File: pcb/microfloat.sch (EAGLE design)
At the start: 130 parts, among them J1 503182-1852, J11 JTAG-MINI, J2 USB4105_REVA, J3 1054291110, J4 1054291110, J5 1054291116, J9 1909763-1, T1 MMBT3906, U1 BME280, U12 TPS54308DDCT, U13 TPS54308DDCT, U2 ICM-42688-P, U3 MAX13237EETE, U4 NEO-M8N-0, U5 TXB0104PWR, U6 LTC4419CMSEPBF, U7 TPS54308DDCT, U8 TPS54308DDCT, U9 ATSAMD51N20A-AUT, Y1 32.768kHz

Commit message: part of component placement done
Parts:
- added C41: 10uF, rcl:CPOL-USE2.5-5
- added C42: 100uF, rcl:CPOL-USE3.5-8
- added C43, C44: 0.1uF, rcl:C-USC0603
- added F6: 0.6A, microfloat:SMD_FUSE1206
- renumbered J11 to J6
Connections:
- removed net GND1: C11.2, C12.2, C29.2, C30.2, C8.2
- new net N$27: C41.+, C42.+, F6.1
- new net N$29: J6.GND@1
- net +3V3: now also C43.1, C44.1
- net GND: now also C11.2, C12.2, C29.2, C30.2, C41.-, C42.-, C43.2, C44.2, C8.2; no longer J6.GND@1
- net VBATT: now also F6.2
- net XIN32: now also U9.PA00
- net XOUT32: now also U9.PA01
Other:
- moved on the sheet: C26, C33, C34, C35, C36, C37, C38, C39, L1

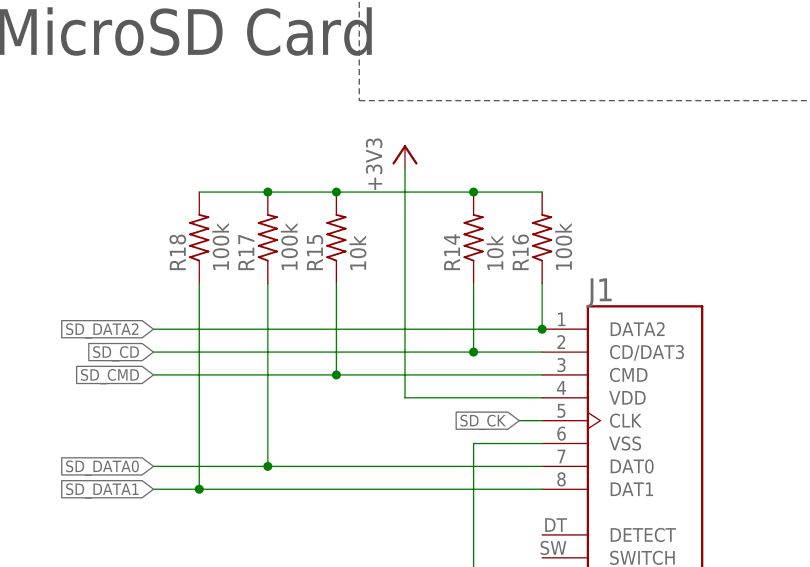
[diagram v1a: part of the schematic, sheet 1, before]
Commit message: component placement near complete, need to fix connector, place test points
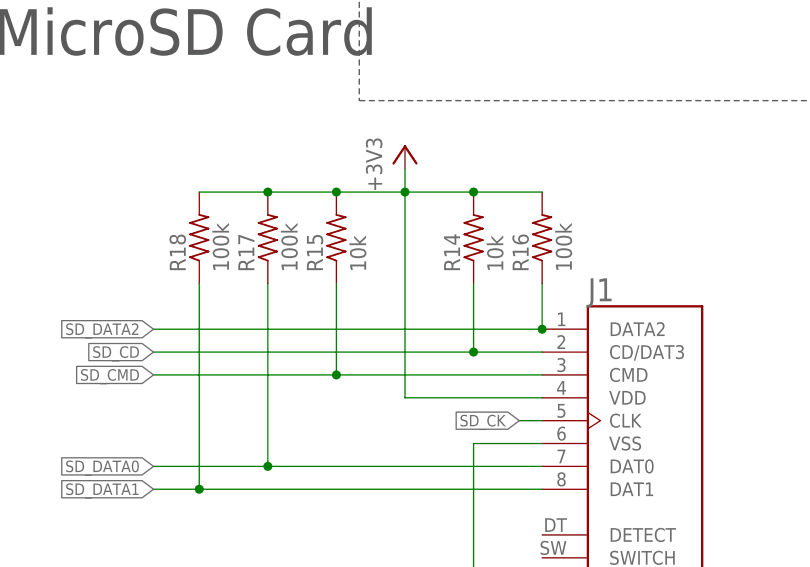
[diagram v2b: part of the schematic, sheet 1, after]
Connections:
- removed net N$25: R14.2, R15.2, R16.2, R17.2, R18.2
- net +3V3: now also R14.2, R15.2, R16.2, R17.2, R18.2
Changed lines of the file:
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@@
 <part name="F5" library="microfloat" deviceset="SMD_FUSE" device="1206" value="0.5A"/>
 <part name="U$29" library="microfloat" deviceset="TEST_POINT" device=""/>
-<part name="U$30" library="microfloat" deviceset="VBATT_5V" device=""/>
 <part name="U$31" library="microfloat" deviceset="TEST_POINT" device=""/>
 <part name="U$32" library="microfloat" deviceset="TEST_POINT" device=""/>
@@
 <part name="J6" library="microfloat" deviceset="JTAG-MINI" device=""/>
 <part name="GND18" library="supply1" library_urn="urn:adsk.eagle:library:371" deviceset="GND" device=""/>
+<part name="U$16" library="microfloat" deviceset="VBATT_5V" device=""/>
 </parts>
 <sheets>
@@
 <pinref part="J1" gate="G$1" pin="VDD"/>
 <wire x1="233.68" y1="187.96" x2="218.44" y2="187.96" width="0.1524" layer="91"/>
-<wire x1="218.44" y1="187.96" x2="218.44" y2="213.36" width="0.1524" layer="91"/>
+<wire x1="218.44" y1="187.96" x2="218.44" y2="210.82" width="0.1524" layer="91"/>
 <pinref part="+3V15" gate="G$1" pin="+3V3"/>
+<pinref part="R16" gate="G$1" pin="2"/>
+<pinref part="R18" gate="G$1" pin="2"/>
+<wire x1="218.44" y1="210.82" x2="218.44" y2="213.36" width="0.1524" layer="91"/>
+<wire x1="233.68" y1="210.82" x2="226.06" y2="210.82" width="0.1524" layer="91"/>
+<pinref part="R14" gate="G$1" pin="2"/>
+<wire x1="226.06" y1="210.82" x2="218.44" y2="210.82" width="0.1524" layer="91"/>
+<junction x="226.06" y="210.82"/>
+<pinref part="R15" gate="G$1" pin="2"/>
+<wire x1="218.44" y1="210.82" x2="210.82" y2="210.82" width="0.1524" layer="91"/>
+<wire x1="210.82" y1="210.82" x2="203.2" y2="210.82" width="0.1524" layer="91"/>
+<junction x="210.82" y="210.82"/>
+<pinref part="R17" gate="G$1" pin="2"/>
+<wire x1="203.2" y1="210.82" x2="195.58" y2="210.82" width="0.1524" layer="91"/>
+<junction x="203.2" y="210.82"/>
+<junction x="218.44" y="210.82"/>
 </segment>
 <segment>
@@
 </segment>
 </net>
-<net name="N$25" class="0">
-<segment>
-<pinref part="R16" gate="G$1" pin="2"/>
-<pinref part="R18" gate="G$1" pin="2"/>
-<wire x1="233.68" y1="210.82" x2="226.06" y2="210.82" width="0.1524" layer="91"/>
-<pinref part="R14" gate="G$1" pin="2"/>
-<wire x1="226.06" y1="210.82" x2="210.82" y2="210.82" width="0.1524" layer="91"/>
-<junction x="226.06" y="210.82"/>
-<pinref part="R15" gate="G$1" pin="2"/>
-<wire x1="210.82" y1="210.82" x2="203.2" y2="210.82" width="0.1524" layer="91"/>
-<junction x="210.82" y="210.82"/>
-<pinref part="R17" gate="G$1" pin="2"/>
-<wire x1="203.2" y1="210.82" x2="195.58" y2="210.82" width="0.1524" layer="91"/>
-<junction x="203.2" y="210.82"/>
-</segment>
-</net>
 <net name="MOSI_1" class="0">
 <segment>
@@
 </instance>
 <instance part="U$29" gate="G$1" x="157.48" y="180.34" smashed="yes"/>
-<instance part="U$30" gate="G$1" x="381" y="264.16" smashed="yes">
-<attribute name="VALUE" x="378.46" y="261.62" size="1.778" layer="96" rot="R90"/>
-</instance>
 <instance part="U$31" gate="G$1" x="241.3" y="149.86" smashed="yes"/>
 <instance part="U$32" gate="G$1" x="284.48" y="157.48" smashed="yes"/>
@@
 <attribute name="VALUE" x="340.36" y="180.34" size="1.778" layer="96" rot="R90"/>
 </instance>
+<instance part="U$16" gate="G$1" x="381" y="264.16" smashed="yes">
+<attribute name="VALUE" x="378.46" y="261.62" size="1.778" layer="96" rot="R90"/>
+</instance>
 </instances>
 <busses>
@@
 </segment>
 </net>
-<net name="N$19" class="0">
-<segment>
-<pinref part="R10" gate="G$1" pin="2"/>
-<wire x1="370.84" y1="238.76" x2="370.84" y2="236.22" width="0.1524" layer="91"/>
-<wire x1="370.84" y1="238.76" x2="381" y2="238.76" width="0.1524" layer="91"/>
-<junction x="370.84" y="238.76"/>
-<pinref part="L2" gate="A" pin="2"/>
-<wire x1="363.22" y1="238.76" x2="370.84" y2="238.76" width="0.1524" layer="91"/>
-<wire x1="381" y1="238.76" x2="381" y2="228.6" width="0.1524" layer="91"/>
-<pinref part="C19" gate="G$1" pin="1"/>
-<wire x1="381" y1="238.76" x2="391.16" y2="238.76" width="0.1524" layer="91"/>
-<wire x1="391.16" y1="238.76" x2="391.16" y2="228.6" width="0.1524" layer="91"/>
-<pinref part="C20" gate="G$1" pin="1"/>
-<junction x="381" y="238.76"/>
-<pinref part="F4" gate="G$1" pin="1"/>
-</segment>
-</net>
 <net name="N$20" class="0">
 <segment>
@@
 </segment>
 <segment>
-<pinref part="F4" gate="G$1" pin="2"/>
-<wire x1="381" y1="261.62" x2="381" y2="259.08" width="0.1524" layer="91"/>
 <pinref part="U$9" gate="G$1" pin="P$1"/>
+<pinref part="F4" gate="G$1" pin="2"/>
+<pinref part="U$16" gate="G$1" pin="VBATT_5V"/>
+<wire x1="381" y1="259.08" x2="381" y2="261.62" width="0.1524" layer="91"/>
 <junction x="381" y="259.08"/>
-<pinref part="U$30" gate="G$1" pin="VBATT_5V"/>
 </segment>
 </net>
@@
 </segment>
 </net>
+<net name="N$19" class="0">
+<segment>
+<wire x1="391.16" y1="238.76" x2="391.16" y2="228.6" width="0.1524" layer="91"/>
+<pinref part="C20" gate="G$1" pin="1"/>
+<pinref part="R10" gate="G$1" pin="2"/>
+<wire x1="370.84" y1="238.76" x2="370.84" y2="236.22" width="0.1524" layer="91"/>
+<pinref part="L2" gate="A" pin="2"/>
+<wire x1="363.22" y1="238.76" x2="370.84" y2="238.76" width="0.1524" layer="91"/>
+<pinref part="C19" gate="G$1" pin="1"/>
+<pinref part="F4" gate="G$1" pin="1"/>
+<wire x1="381" y1="228.6" x2="381" y2="238.76" width="0.1524" layer="91"/>
+<wire x1="370.84" y1="238.76" x2="381" y2="238.76" width="0.1524" layer="91"/>
+<junction x="370.84" y="238.76"/>
+<junction x="381" y="238.76"/>
+<wire x1="391.16" y1="238.76" x2="381" y2="238.76" width="0.1524" layer="91"/>
+</segment>
+</net>

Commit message: Work in progress
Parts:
- removed L1: 380hm, RoboJackets-Inductors:INDUCTOR_0805
- added C45, C46: 0.1uF, rcl:C-USC0603
- C15, C16: value 15 pF -> 8.2 pF
- C41, C42: TOLERANCE (none) -> 20%; VOLTAGE (none) -> 35V
- F6: value 0.6A -> 3A
- R1: TOLERANCE (none) -> 1%
- R8, R9: TOLERANCE 1% -> 0.1%
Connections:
- removed net N$29: J6.GND@1
- removed net N$30: J4.11
- net +3V3: now also C36.1, C37.1, C45.1, C46.1; no longer L1.1
- net GND: now also C45.2, C46.2, J4.11, J6.GND@1
- net VCCA: no longer C36.1, C37.1, L1.2

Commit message: Put final crystal part
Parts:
- added C47: 10uF, rcl:C-USC0603
- added C48: 0.1uF, rcl:C-USC0603
- added L1: FB-30Ohm, RoboJackets-Inductors:INDUCTOR_0805
- added L4: 10uH, RoboJackets-Inductors:INDUCTOR_0805
- C15, C16: TOLERANCE (none) -> 0.5%; VOLTAGE (none) -> 10V
- C32, C33, C34, C43, C44: TOLERANCE (none) -> 5%; VOLTAGE (none) -> 10V
- C36: value 0.1uF -> 10uF
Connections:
- new net GND1: C47.2
- new net GND2: C48.2
- new net N$25: L4.1, U9.VSW
- net +3V3: now also L1.1
- net VCCA: now also C47.1, C48.1, L1.2
- net VCC_CORE: now also L4.2
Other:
- moved on the sheet: C38, C39

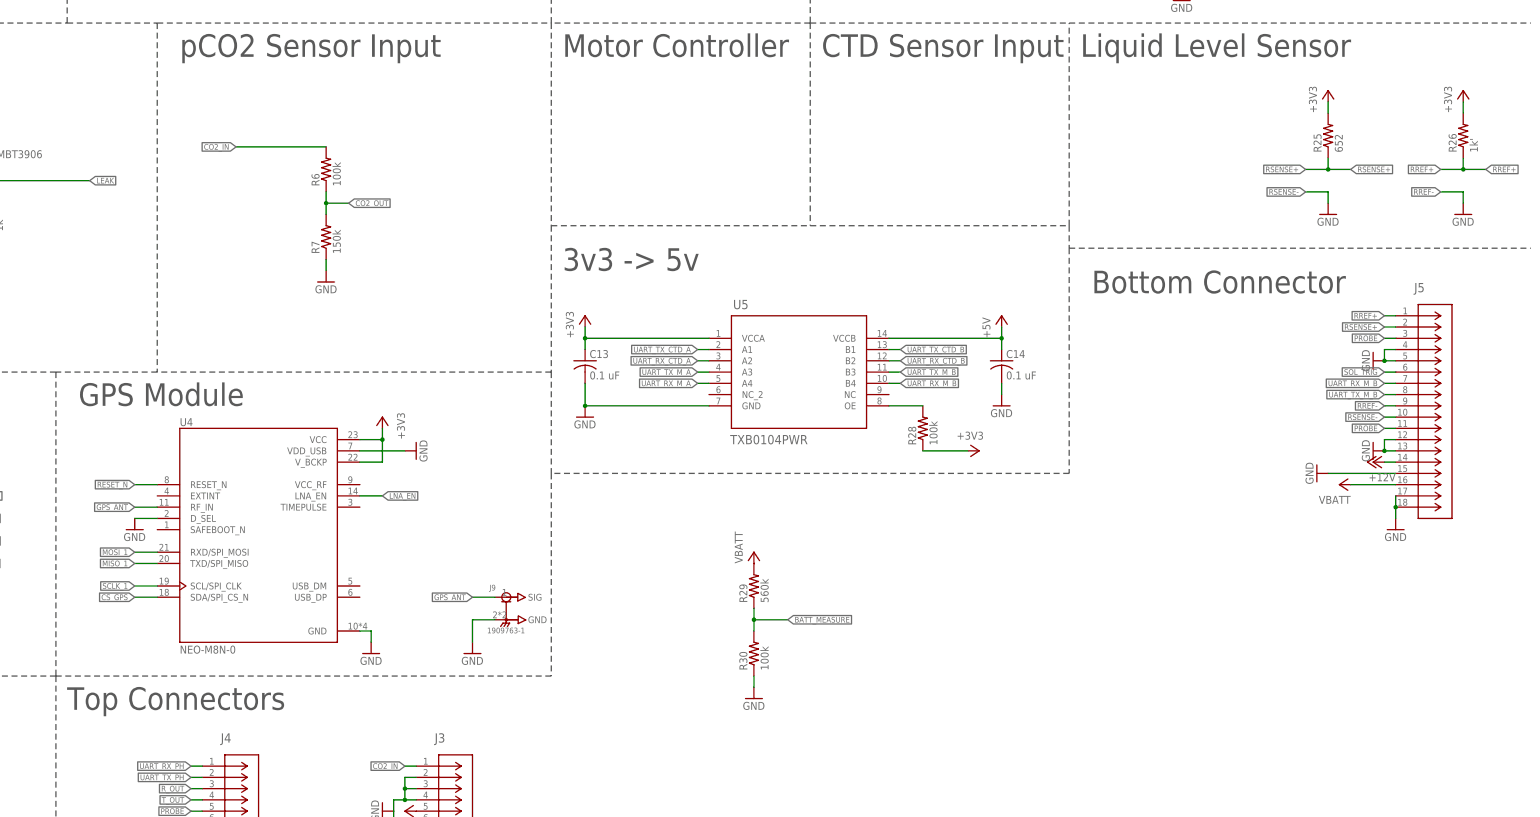
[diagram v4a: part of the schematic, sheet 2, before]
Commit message: Final schematic with missing passives
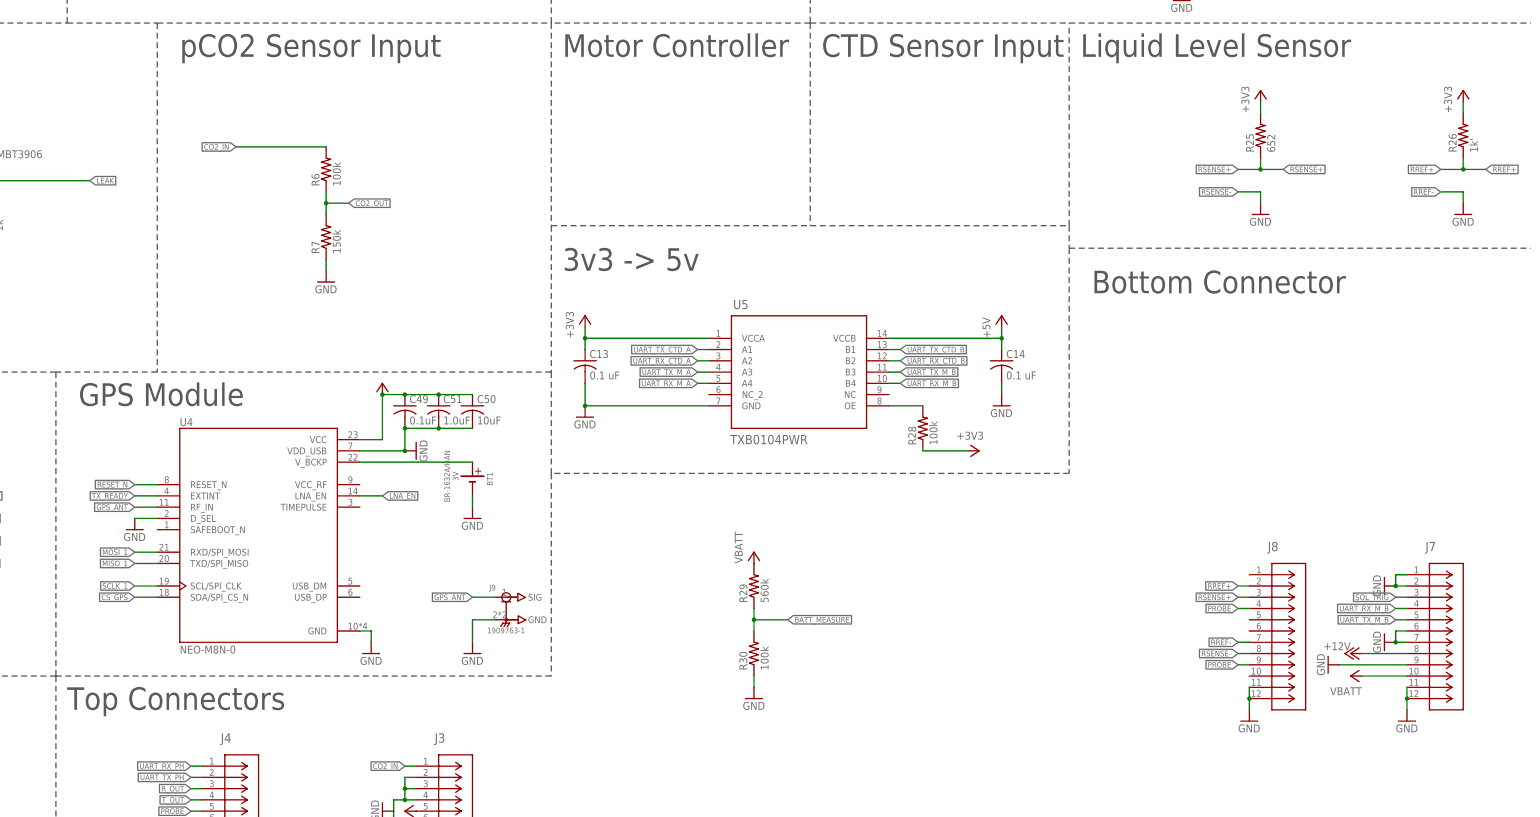
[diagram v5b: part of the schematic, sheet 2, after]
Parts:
- removed C56: 22uF, rcl:C-USC0603
- removed J5: 1054291116, microfloat:1054291116
- removed S2: KMR2, RoboJackets-Switches:KMR2
- added BT1: BATTERY, microfloat:BATTERY
- added C49: 0.1uF, rcl:C-USC0603
- added C50: 10uF, rcl:C-USC0603
- added C51: 1.0uF, rcl:C-USC0603
- added C52: 22uF, rcl:C-USC0603
- added J7, J8: 1054291110, microfloat:1054291110
- added R35: 330, rcl:R-US_R0603
- added S1: (no value), microfloat:BTN_10-XXSMD
- C26, C35, C36, C37, C38, C39, C45, C46, C47, C48, C6: TOLERANCE (none) -> 5%; VOLTAGE (none) -> 10V
- C41, C42: VOLTAGE 35V -> 25V
- C55: TOLERANCE (none) -> 5%; VOLTAGE (none) -> 16V
- L1: DKPN (none) -> 490-1035-1-ND; TOLERANCE 10% -> 25%
- R19: value 10k -> 1k
- Y1: value 32.768kHz -> ABS25-32.768KHZ-6-1-T; device microfloat:CRYSTAL5X3 -> microfloat:ABS25-32.768KHZ-6-1-T
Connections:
- removed net GND1: C47.2
- removed net GND2: C48.2
- new net !RESET!: R35.2
- new net N$29: R35.1, S1.P
- new net N$30: J8.11
- new net N$31: J7.11
- new net N$32: BT1.PLUS, U4.V_BCKP
- new net TX_READY: U4.EXTINT, U9.PB22
- net !RESET: no longer S2.1
- net +12V: now also J7.8; no longer J5.14
- net +3V3: now also C49.1, C50.1, C51.1; no longer U4.V_BCKP
- net GND: now also BT1.MINUS, C47.2, C48.2, C49.2, C50.2, C51.2, C52.2, J7.1, J7.12, J7.2, J7.6, J7.7, J7.9, J8.12, S1.S; no longer C56.2, J5.12, J5.13, J5.15, J5.17, J5.18, J5.4, J5.5, S2.2
- net N$17: now also C52.1; no longer C56.1
- net PROBE: now also J8.4, J8.9; no longer J5.11, J5.3
- net RREF+: now also J8.2; no longer J5.1
- net RREF-: now also J8.7; no longer J5.9
- net RSENSE+: now also J8.3; no longer J5.2
- net RSENSE-: now also J8.8; no longer J5.10
- net SOL_TRIG: now also J7.3; no longer J5.6
- net UART_RX_M_B: now also J7.4; no longer J5.7
- net UART_TX_M_B: now also J7.5; no longer J5.8
- net VBATT: now also J7.10; no longer J5.16
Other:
- moved on the sheet: C26, C35, C36, C37, C45, C46, C55, R25

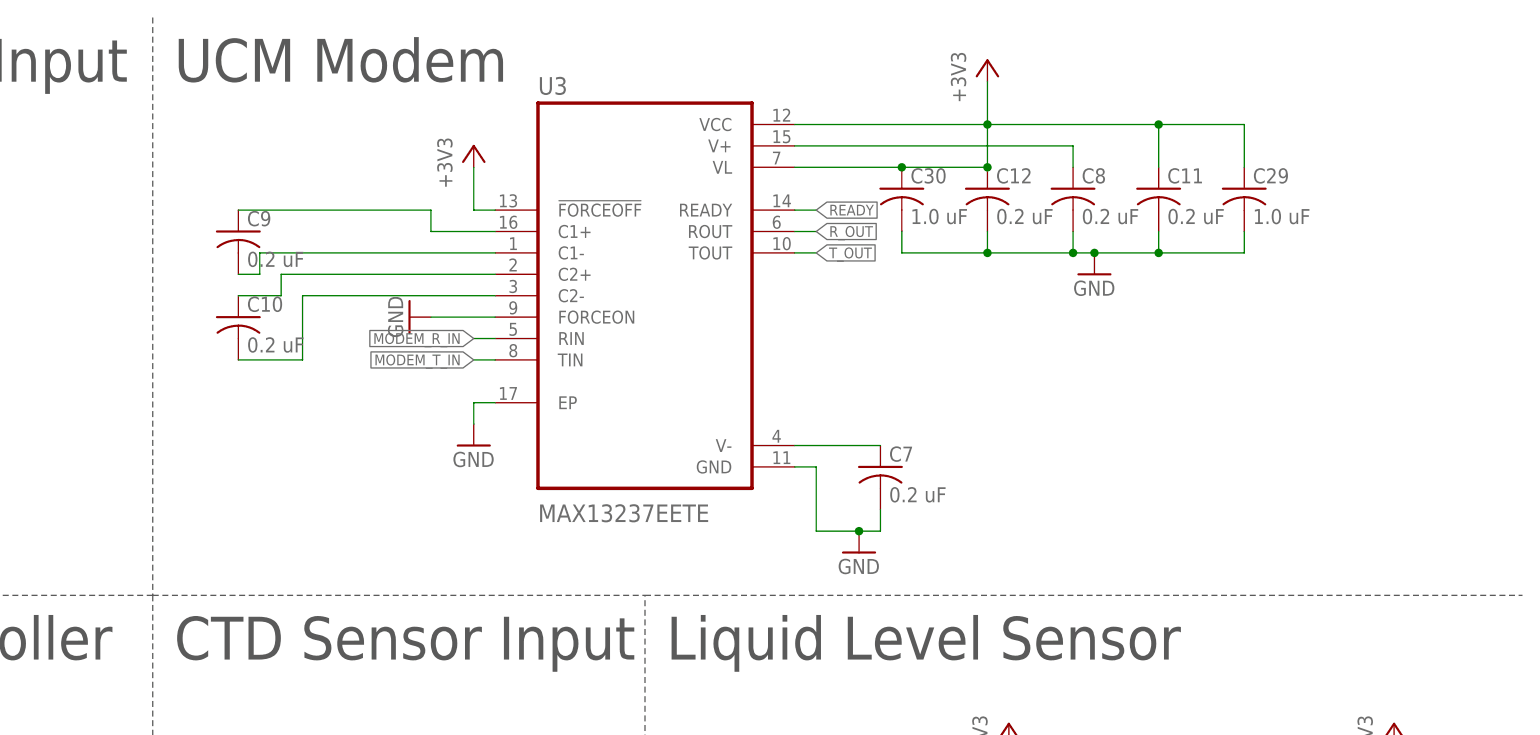
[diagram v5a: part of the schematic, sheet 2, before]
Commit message: Swapped capcitors into parallel
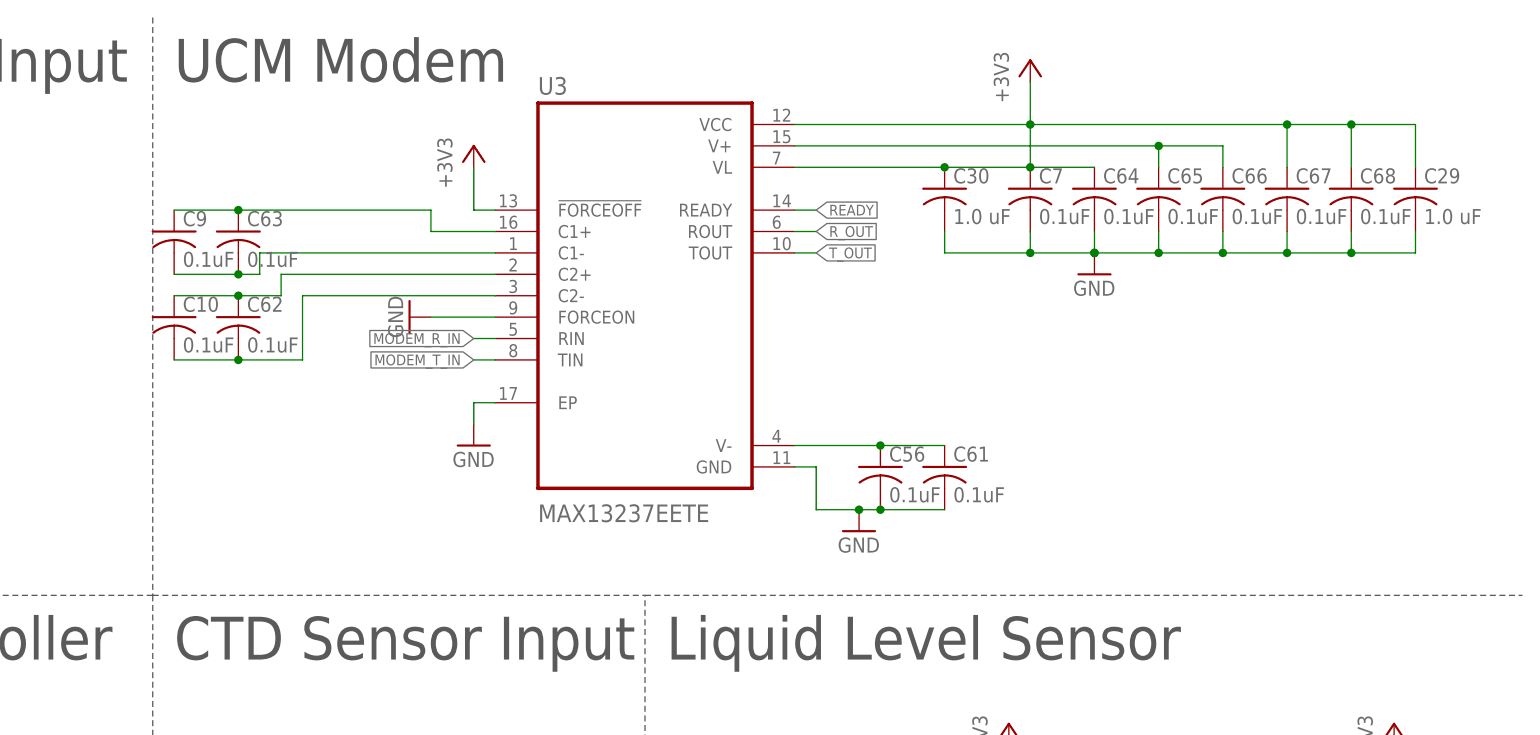
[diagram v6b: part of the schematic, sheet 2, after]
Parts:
- removed C12, C8: 0.2 uF, rcl:C-USC0603
- added C56, C61, C62, C63, C64, C66, C67, C68: 0.1uF, rcl:C-USC0603
- C10, C65, C7, C9: value 0.2 uF -> 0.1uF; TOLERANCE 1% -> 5%
- renumbered C11 to C65
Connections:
- net +3V3: now also C64.1, C67.1, C68.1, C7.1; no longer C12.1, C65.1
- net GND: now also C56.2, C61.2, C64.2, C66.2, C67.2, C68.2; no longer C12.2, C8.2
- net N$10: now also C65.1, C66.1; no longer C8.1
- net N$2: now also C63.1
- net N$4: now also C63.2
- net N$5: now also C62.1
- net N$6: now also C62.2
- net N$8: now also C56.1, C61.1; no longer C7.1
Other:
- moved on the sheet: C10, C29, C30, C7, C9
